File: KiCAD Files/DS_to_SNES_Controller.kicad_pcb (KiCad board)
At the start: 6 copper layers, 141.1 x 77.5 mm, 44 parts, among them J1 Conn_01x01_Pin, J2 Conn_01x01_Pin, J3 Conn_01x01_Pin, J4 Conn_01x01_Pin, J5 Conn_01x01_Pin, U2 4021, U3 4021

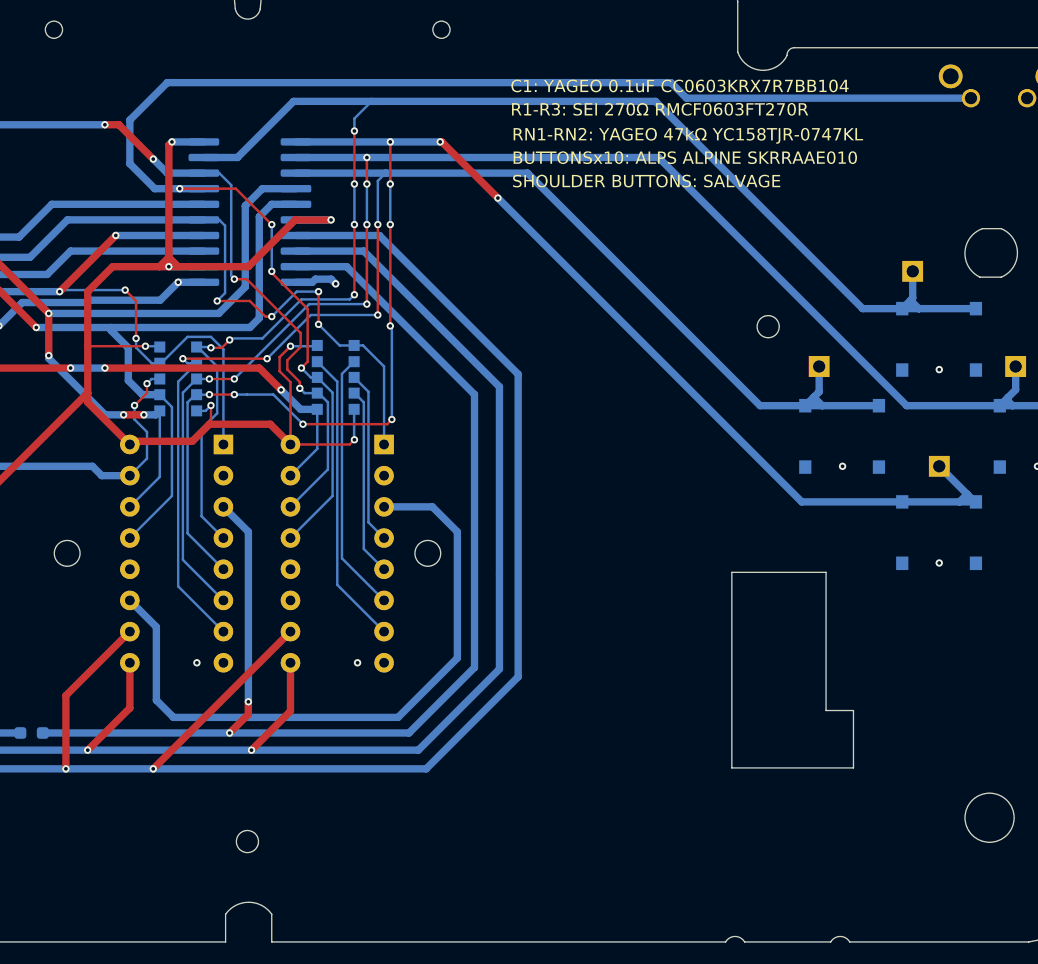
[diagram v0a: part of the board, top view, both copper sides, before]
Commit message: Changed total layers to 2
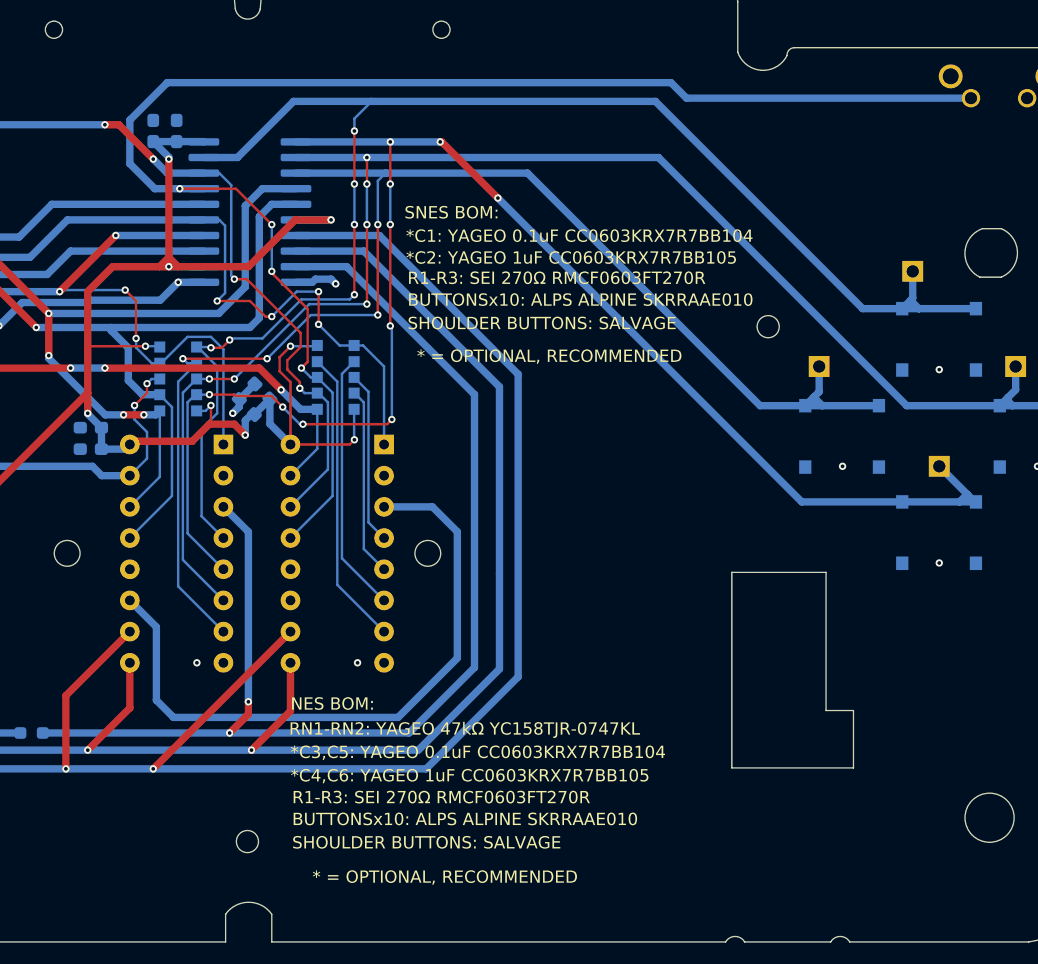
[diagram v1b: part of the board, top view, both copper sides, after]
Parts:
- added C1: 0.1uF, Capacitor_SMD:C_0603_1608Metric_Pad1.08x0.95mm_HandSolder, B.Cu at (140.5, 77.7)
- added C2: 1uF, Capacitor_SMD:C_0603_1608Metric_Pad1.08x0.95mm_HandSolder, B.Cu at (142.4, 77.7)
- added C3: 0.1uF, Capacitor_SMD:C_0603_1608Metric_Pad1.08x0.95mm_HandSolder, B.Cu at (135.4, 101.9)
- added C4: 1uF, Capacitor_SMD:C_0603_1608Metric_Pad1.08x0.95mm_HandSolder, B.Cu at (135.4, 103.6)
- added C5: 0.1uF, Capacitor_SMD:C_0603_1608Metric_Pad1.08x0.95mm_HandSolder, B.Cu at (149.4, 98.9)
- added C6: 1uF, Capacitor_SMD:C_0603_1608Metric_Pad1.08x0.95mm_HandSolder, B.Cu at (148.1, 100.2)
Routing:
- net +5V: track 159.8 -> 167.3 mm, vias 7 -> 9
- net GND: track 21.7 -> 24.8 mm, vias 15 -> 16
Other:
- copper layers 6 -> 2
- board text added: "* = OPTIONAL, RECOMMENDED"
- board text added: "*C1: YAGEO 0.1uF CC0603KRX7R7BB104"
- board text added: "*C2: YAGEO 1uF CC0603KRX7R7BB105"
- board text added: "*C3,C5: YAGEO 0.1uF CC0603KRX7R7BB104"
- board text added: "*C4,C6: YAGEO 1uF CC0603KRX7R7BB105"
- board text added: "- Adam Billingsley"
- board text added: "NES BOM:"
- board text added: "SNES BOM:"
- board text removed: "C1: YAGEO 0.1uF CC0603KRX7R7BB104"
